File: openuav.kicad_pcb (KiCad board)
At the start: 4 copper layers, 36 x 36 mm, 70 parts, among them J1 Conn_01x01, J10 Conn_01x01, J11 Conn_01x01, J12 Conn_01x01, J13 Conn_01x01, J14 Conn_01x01, J15 Conn_01x01, J16 Conn_01x01, J17 Conn_01x01, J18 Conn_01x01, J19 Conn_01x01, J2 Conn_01x01, J20 Conn_01x01, J21 Conn_01x01, J22 Conn_01x01, J23 Conn_01x01, J24 Conn_01x01, J25 Conn_01x01, J26 Conn_01x01, J27 Conn_01x01, J28 Conn_01x01, J29 Conn_01x01, J3 Conn_01x01, J30 Conn_01x01, J31 Conn_01x01, J4 Conn_01x01, J5 Conn_01x01, J6 Conn_01x01, J7 Conn_01x01, J8 Conn_01x01, J9 Conn_01x01, J99 USB_C_Receptacle_USB2.0, U1 STM32G474CETx, U2 BMI270, U3 BMP280, U4 W25Q128JVS, U5 TPS54202DDC, U6 W25N01GVZEIG, U7 XC6206P332MR

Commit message: routing
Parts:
- removed C3: 47u, Capacitor_SMD:C_1206_3216Metric
- moved R4 64.8 mm to (157.4, 75.3), turned to 180 degrees
- moved R3 64.7 mm to (157.4, 74.3)
- moved R6 59.5 mm to (148.6, 80.4), turned to 180 degrees
- moved R5 54.9 mm to (150.6, 80.4), turned to 180 degrees
- moved C10 51.5 mm to (157.4, 76.3), turned to 180 degrees
- moved C9 48.2 mm to (152.9, 78.7), turned to 90 degrees
- moved C2 41.4 mm to (154.0, 75.1)
- moved C14 38.0 mm to (146.6, 80.4)
- moved U5 4.90 mm to (156.2, 78.7)
- moved J19 2.50 mm to (158.5, 52.5)
- moved J20 2.50 mm to (156.0, 52.5)
- moved L1 2.28 mm to (149.2, 76.8)
- moved C13 0.80 mm to (156.8, 59.2)
- moved C8 0.80 mm to (158.9, 61.2)
- moved U3 0.80 mm to (156.8, 61.1)
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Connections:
- U1 pad 5: VOLTAGE -> CURRENT
- U1 pad 6: CURRENT -> VOLTAGE
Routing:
- net UART_1_RX: track 0.00 -> 24.1 mm, vias 0 -> 1
- net UART_2_TX: track 0.00 -> 22.4 mm, vias 0 -> 1
- net CURRENT: track 0.00 -> 21.8 mm
- net UART_1_TX: track 0.00 -> 21.6 mm, vias 0 -> 1
- net PWM_4: track 0.00 -> 20.6 mm, vias 0 -> 1
- net PWM_3: track 0.00 -> 20.0 mm, vias 0 -> 1
- net UART_2_RX: track 0.00 -> 19.8 mm, vias 0 -> 1
- net PWM_1: track 0.00 -> 18.7 mm, vias 0 -> 1
- net PWM_2: track 0.00 -> 18.6 mm, vias 0 -> 1
- net VOLTAGE: track 0.00 -> 17.6 mm
- net UART_4_TX: track 0.00 -> 17.5 mm
- net UART_4_RX: track 0.00 -> 14.7 mm
- net I2C_SDA: track 0.00 -> 13.9 mm
- net I2C_CLK: track 0.00 -> 13.1 mm
- net UART_3_TX: track 0.00 -> 12.5 mm, vias 0 -> 1
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
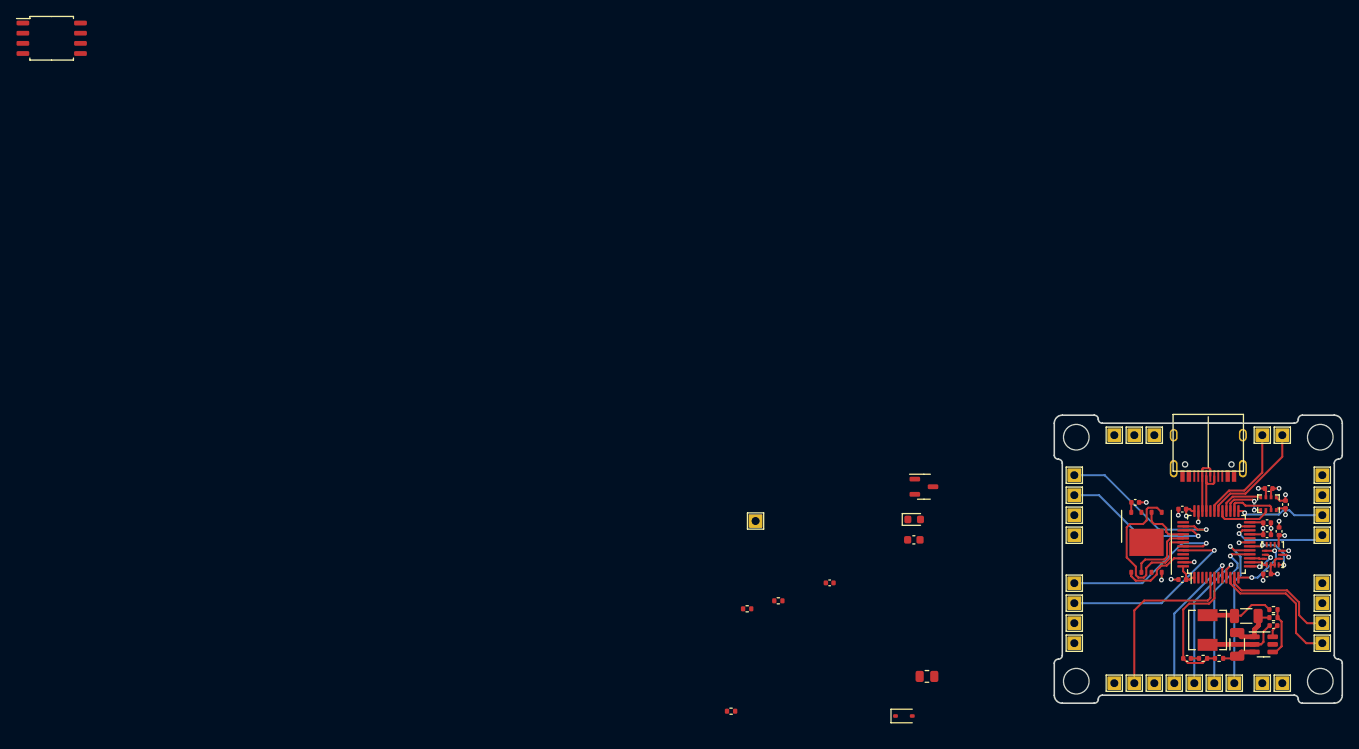
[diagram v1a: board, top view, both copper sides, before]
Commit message: continues work on G474 layout TODO: the pin space is 2.5mm not 2.54mm
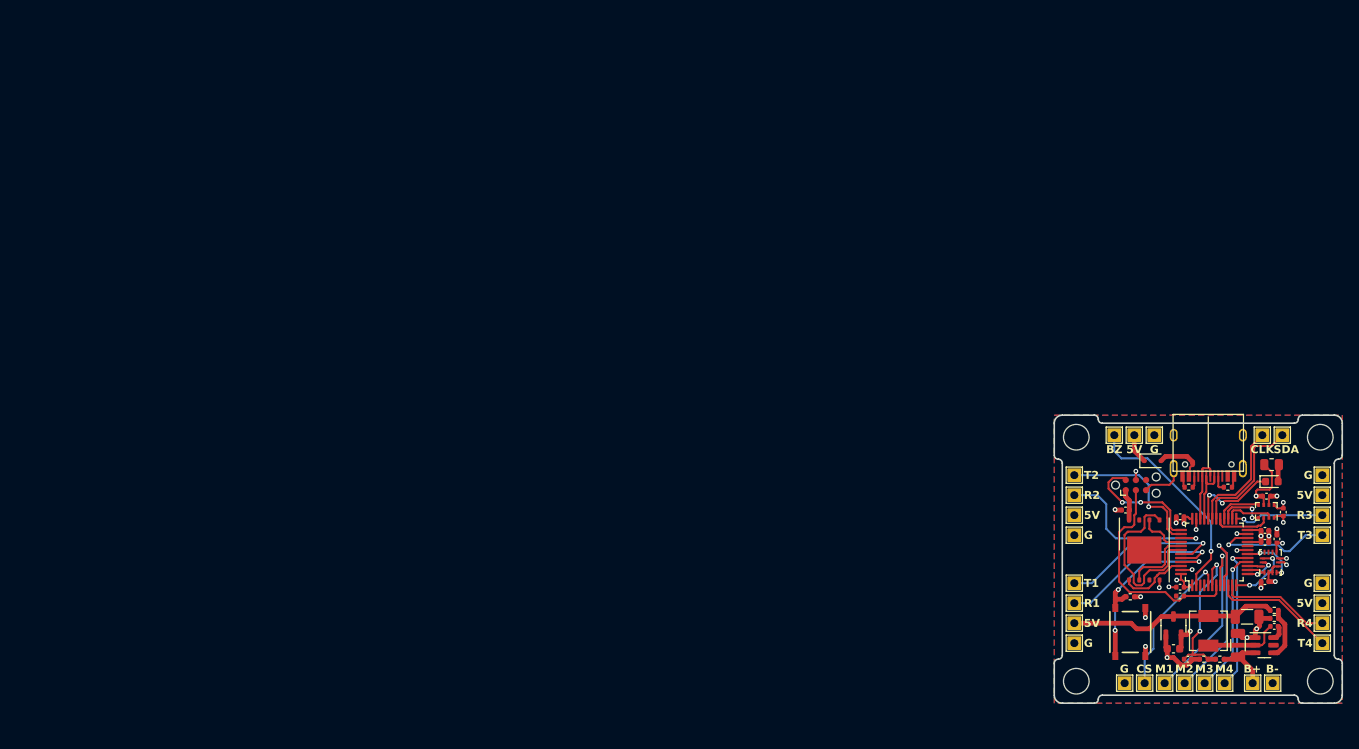
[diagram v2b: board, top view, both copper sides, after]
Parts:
- removed J18: Conn_01x01, Connector_Custom_Pads:TP-2.54
- removed U4: W25Q128JVS, Package_SO:SOIC-8_5.23x5.23mm_P1.27mm
- added SW1: SW_Push, Connector_Custom_Pads:TS-1187A-B-A-B, F.Cu at (139.5, 77.1)
- J17: value Conn_01x01 -> Conn_ARM_SWD_TagConnect_TC2030-NL; footprint Connector_Custom_Pads:TP-2.54 -> Connector:Tag-Connect_TC2030-IDC-NL_2x03_P1.27mm_Vertical
- moved R2 62.0 mm to (151.7, 59.0)
- moved R1 53.2 mm to (146.8, 59.0), turned to 180 degrees
- moved R8 51.9 mm to (139.5, 72.7)
- moved R7 50.6 mm to (157.2, 56.2)
- moved D2 45.0 mm to (157.2, 58.3)
- moved D1 44.6 mm to (142.3, 55.7)
- moved C1 43.8 mm to (145.7, 72.6)
- moved U7 35.7 mm to (144.9, 76.3), turned to 90 degrees
- moved C15 35.2 mm to (144.9, 79.2), turned to 180 degrees
- moved J17 24.9 mm to (140.2, 58.7)
- moved C16 1.55 mm to (138.9, 61.9), turned to 180 degrees
- moved J21 1.30 mm to (138.8, 83.5)
- moved J26 1.30 mm to (141.3, 83.5)
- moved J22 1.20 mm to (143.8, 83.5)
- moved J23 1.20 mm to (146.3, 83.5)
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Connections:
- J17 pad 1: GND -> +3V3
- J8 pad 1: UART_2_TX -> SWCLK
- U1 pad 38: UART_2_TX -> SWCLK
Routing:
- net NRST: track 0.00 -> 27.4 mm
- net BUZZER: track 0.00 -> 26.5 mm, vias 0 -> 1
- net BOOT0: track 0.00 -> 26.3 mm, vias 0 -> 3
- net UART_2_TX: track 22.4 -> 0.00 mm, vias 1 -> 0
- net +5V: track 8.53 -> 30.0 mm
- net SWCLK: track 0.00 -> 20.9 mm, vias 0 -> 2
- net +3V3: track 21.0 -> 39.0 mm, vias 6 -> 10
- net GND: track 26.0 -> 43.4 mm, vias 15 -> 19
- net SWDIO: track 0.00 -> 15.7 mm, vias 0 -> 2
- net LED: track 0.00 -> 11.5 mm, vias 0 -> 2
- net PWM_2: track 18.6 -> 25.3 mm
- net Net-(D1-A): track 0.00 -> 6.36 mm
- net +BATT: track 4.25 -> 8.38 mm
- net PWM_1: track 18.7 -> 22.6 mm
- net UART_3_TX: track 12.5 -> 15.6 mm
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- added copper zone on B.Cu, net (none)
- added copper zone on F.Cu, net (none)
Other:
- board text added: "5V"
- board text added: "B+"
- board text added: "B-"
- board text added: "BZ"
- board text added: "CLK"
- board text added: "CS"
- board text added: "G"
- board text added: "M1"
- board text added: "M2"
- board text added: "M3"
- board text added: "M4"
- board text added: "R1"
- board text added: "R2"
- board text added: "R3"
- board text added: "R4"
- board text added: "SDA"
- board text added: "T1"
- board text added: "T2"
- board text added: "T3"
- board text added: "T4"

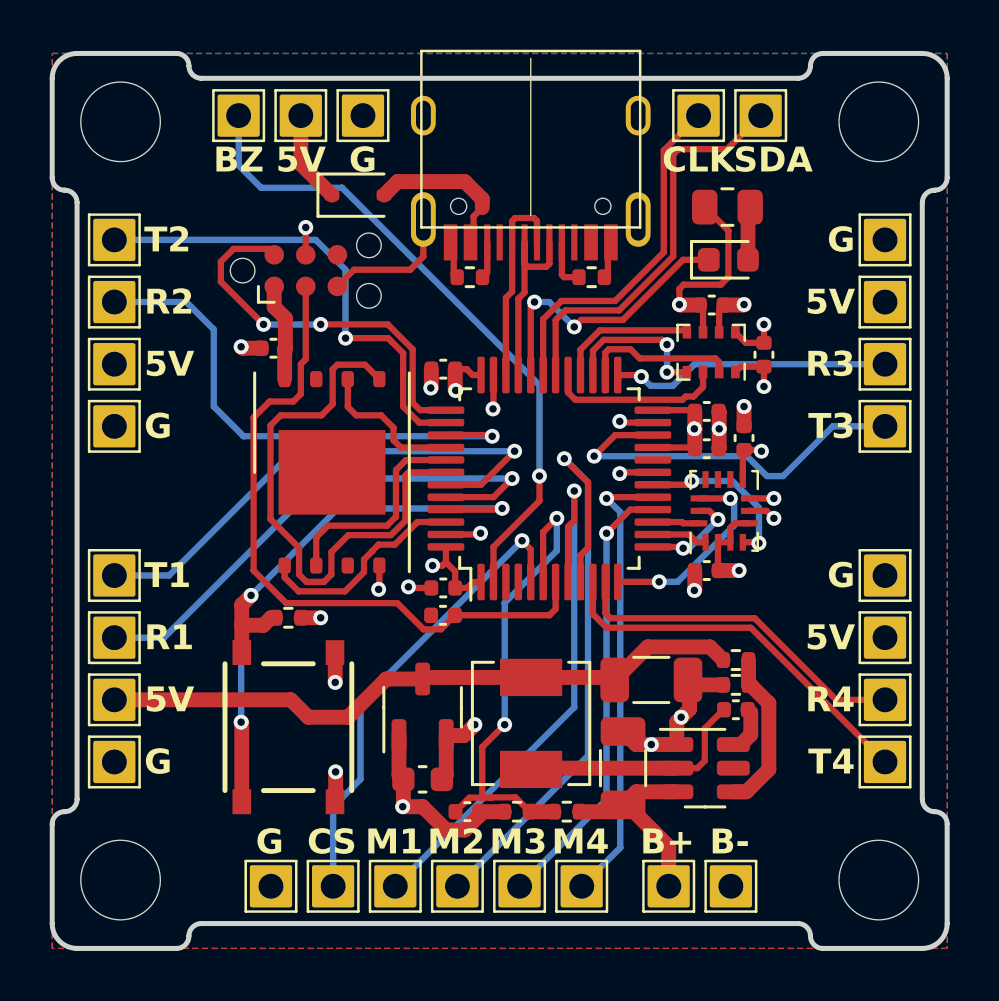
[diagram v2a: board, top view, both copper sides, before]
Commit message: finish G474 layout, add buzzer buffer, add pullups, fix pin spacing
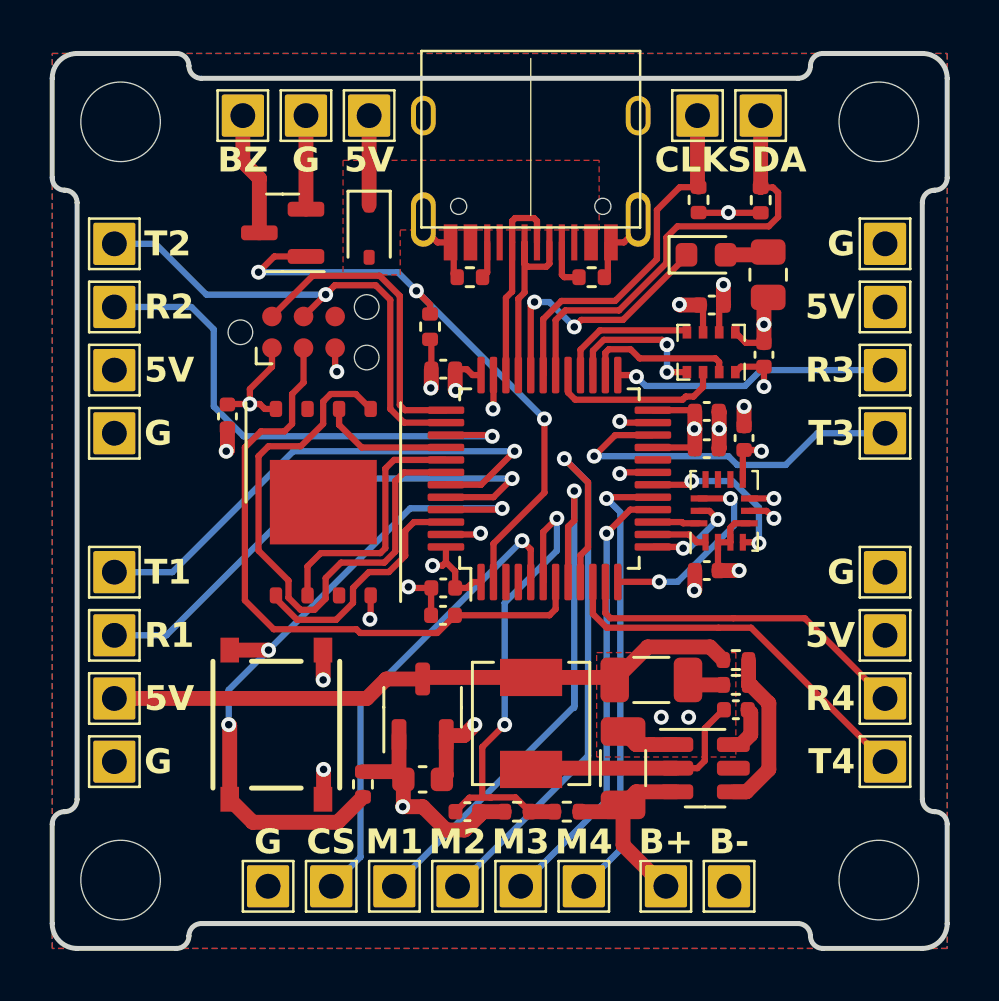
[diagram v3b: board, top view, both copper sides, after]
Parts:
- added Q2: AO3400A, Package_TO_SOT_SMD:SOT-23, F.Cu at (139.3, 57.2)
- added R10: 10k, Resistor_SMD:R_0402_1005Metric, F.Cu at (156.0, 55.9)
- added R11: 10k, Resistor_SMD:R_0402_1005Metric, F.Cu at (145.2, 61.0)
- added R9: 10k, Resistor_SMD:R_0402_1005Metric, F.Cu at (158.5, 55.9)
- moved R8 7.34 mm to (142.5, 79.4), turned to 90 degrees
- moved C16 3.31 mm to (137.1, 64.6), turned to -90 degrees
- moved R7 3.17 mm to (158.8, 58.9), turned to 90 degrees
- moved J28 2.75 mm to (142.7, 52.5)
- moved J17 2.48 mm to (140.1, 61.2)
- moved J27 2.29 mm to (140.2, 52.5)
- moved D1 1.52 mm to (142.7, 57.1), turned to -90 degrees
- moved U6 1.25 mm to (140.9, 68.0)
- moved D2 0.92 mm to (156.3, 58.1)
- moved SW1 0.49 mm to (139.0, 77.0)
- moved J12 0.28 mm to (163.5, 65.3)
- moved J5 0.28 mm to (132.5, 65.3)
- moved J11 0.24 mm to (163.5, 62.7)
- moved J6 0.24 mm to (132.5, 62.7)
- moved J10 0.20 mm to (163.5, 60.2)
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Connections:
- J29 pad 1: BUZZER -> BZ
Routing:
- net Net-(D1-A): track 6.36 -> 0.00 mm
- net BZ: track 0.00 -> 4.99 mm
- net +3V3: track 39.0 -> 34.3 mm, vias 10 -> 12
- net PWM_2: track 25.3 -> 28.6 mm
- net SWDIO: track 15.7 -> 12.5 mm, vias 2 -> 0
- net BOOT0: track 26.3 -> 28.4 mm
- net I2C_SDA: track 16.3 -> 18.1 mm
- net BUZZER: track 26.5 -> 24.7 mm, vias 1 -> 3
- net GND: track 43.4 -> 45.1 mm
- net SPI3_MISO: track 8.74 -> 10.4 mm
- net SPI3_CS: track 8.66 -> 9.89 mm
- net NRST: track 27.4 -> 26.2 mm
- net PWM_1: track 22.6 -> 23.8 mm
- net SPI3_MOSI: track 22.4 -> 23.5 mm
- net LED: track 11.5 -> 10.8 mm
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- added copper zone on In2.Cu, net +5V
- added copper zone on F.Cu, net GND
- added copper zone on F.Cu, net Net-(D1-A)
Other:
- board text added: "JLCJLCJLCJLC"
- board text added: "OPENUAV v0.1"

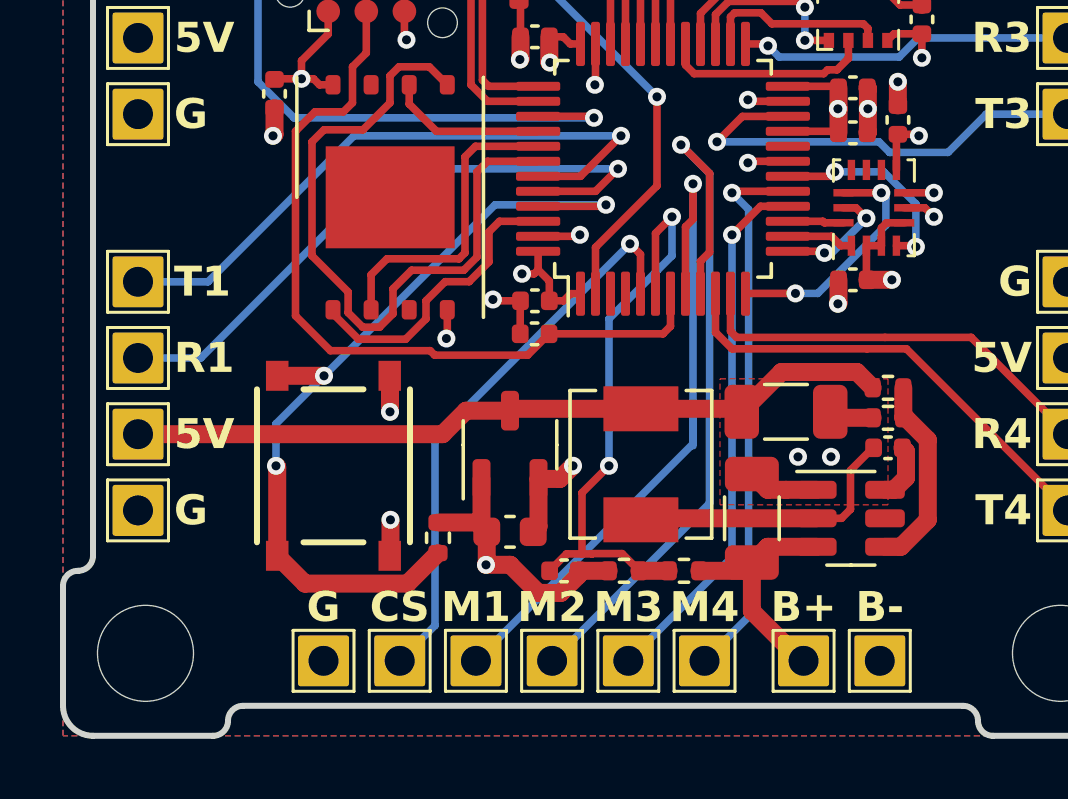
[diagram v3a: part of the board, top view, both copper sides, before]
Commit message: add heatsink copper to inductor
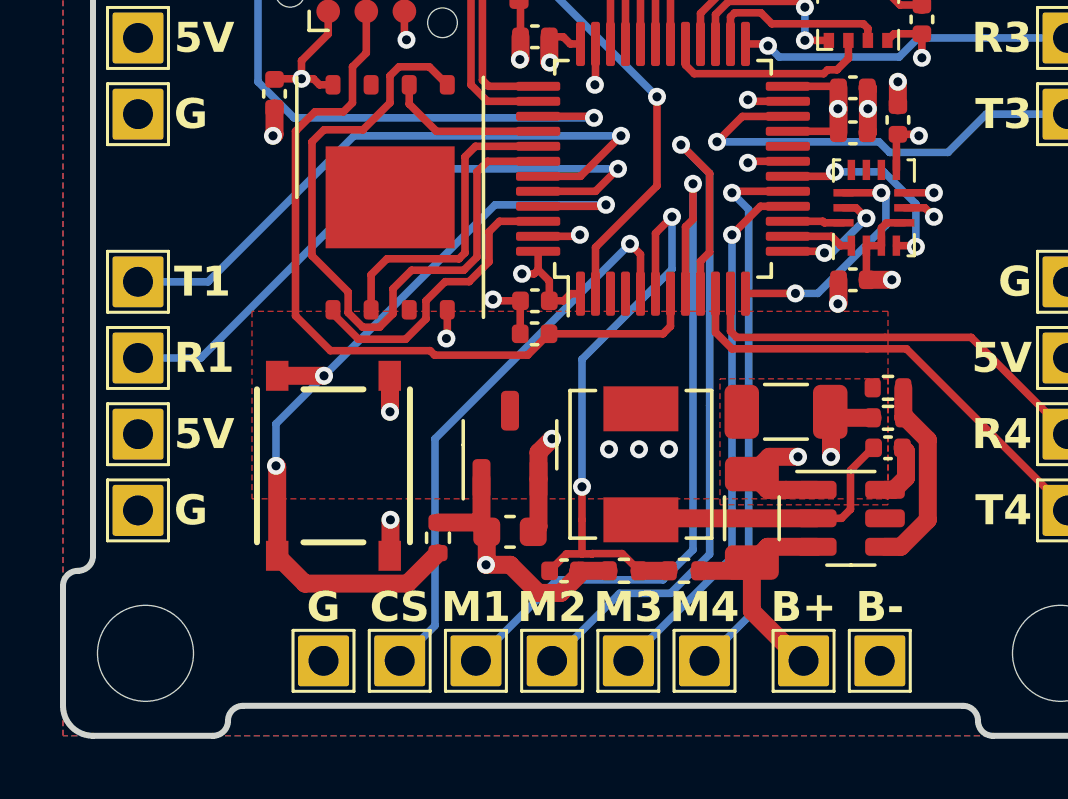
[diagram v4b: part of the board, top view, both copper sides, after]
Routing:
- net +5V: track 29.3 -> 3.60 mm, vias 0 -> 3
- net GND: track 45.1 -> 48.1 mm
- net PWM_2: track 28.6 -> 26.2 mm
- net PWM_1: track 23.8 -> 24.7 mm
- added copper zone on F.Cu, net +5V
